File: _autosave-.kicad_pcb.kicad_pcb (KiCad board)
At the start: 2 copper layers, 42 parts, among them P2 CONN_6, P3 CONN_2, P4 CONN_2, P5 CONN_01X02, P6 CONN_01X12, SW1 SW_PUSH, SW2 SW_PUSH, SW3 SW_PUSH, U1 STM32F411RE_LQFP64, U3 LM1084IS-3.3/NOPB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

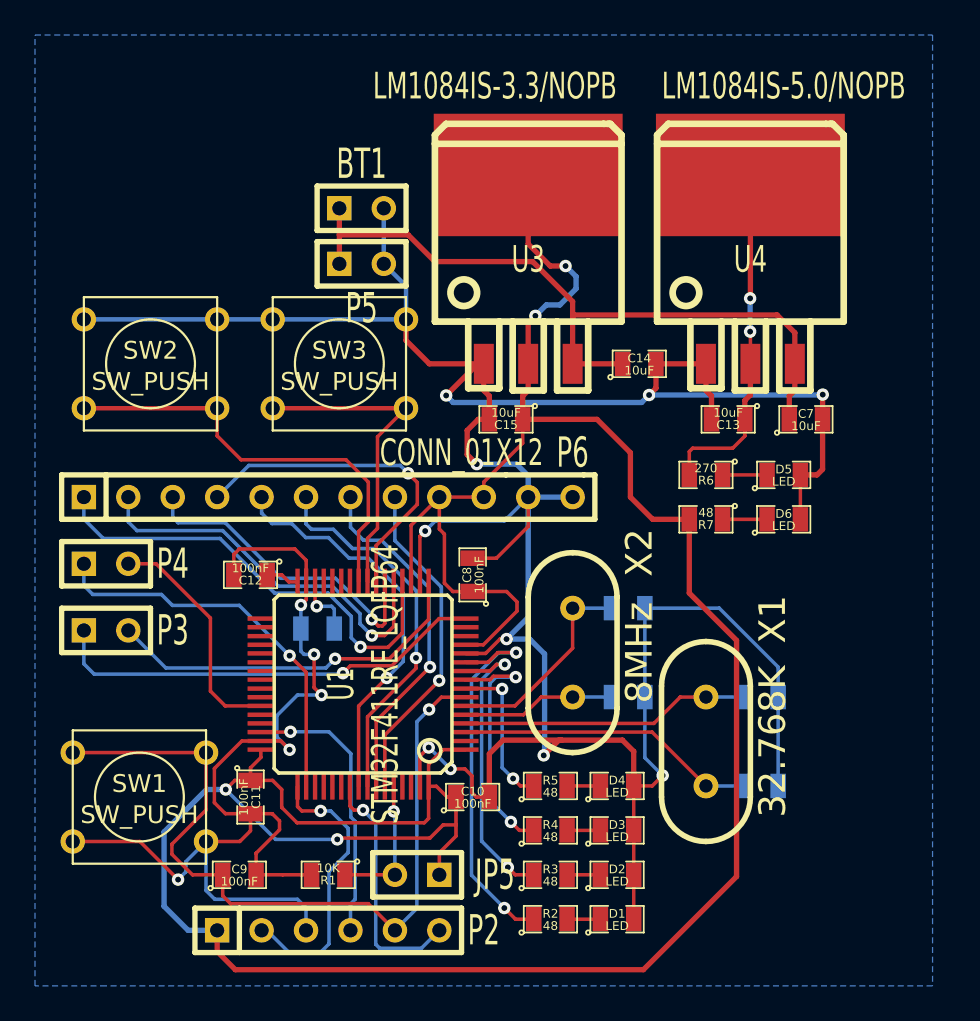
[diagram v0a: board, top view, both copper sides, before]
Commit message: Changed stuff
Layed out board with regulators, leds, and GPIOs
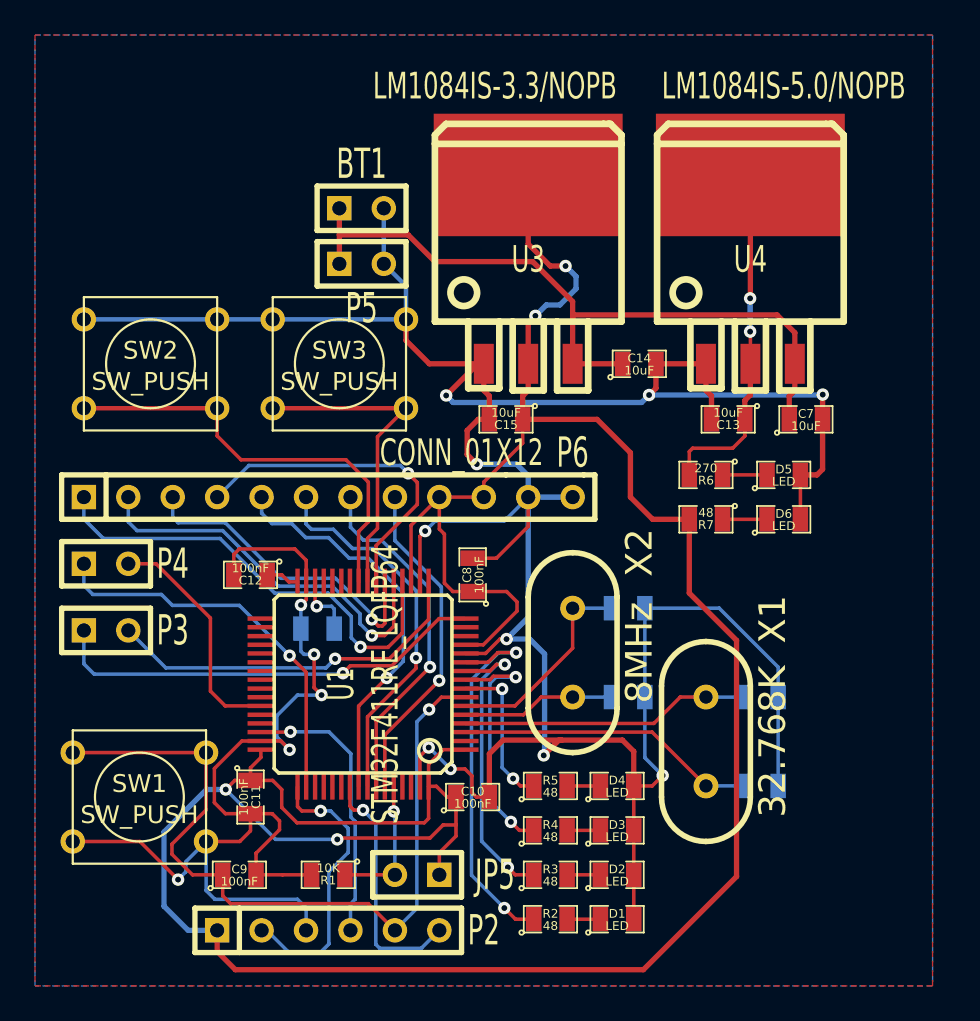
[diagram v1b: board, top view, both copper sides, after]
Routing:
- added copper zone on F.Cu, net 3V3
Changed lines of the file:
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@@
   (general
     (links 107)
-    (no_connects 1)
-    (area 0 0 0 0)
+    (no_connects 0)
+    (area 69.596 47.244 122.269955 101.600001)
     (thickness 1.6)
     (drawings 0)
@@
       )
     )
+  )
+  (zone (net 25) (net_name 3V3) (layer F.Cu) (hatch edge 0.508)
+    (connect_pads (clearance 0.508))
+    (min_thickness 0.254)
+    (fill (arc_segments 16) (thermal_gap 0.508) (thermal_bridge_width 0.508))
+    (polygon
+      (pts
+        (xy 120.904 101.6) (xy 120.904 47.244) (xy 69.596 47.244) (xy 69.596 101.6) (xy 118.364 101.6)
+      )
+    )
